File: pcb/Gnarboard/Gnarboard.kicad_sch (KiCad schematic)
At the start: 2 parts, among them U2 MCP3208

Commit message: a bit more progress on the design. kicad pretty decent these days.
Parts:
- added C1: 100nF, Capacitor_THT:C_Disc_D4.7mm_W2.5mm_P5.00mm, symbol Device:C_Small
- added C2: 100uF, Capacitor_THT:CP_Radial_D8.0mm_P5.00mm, symbol Device:C_Polarized_Small
- added D1: 30V, Diode_THT:D_DO-35_SOD27_P10.16mm_Horizontal, symbol Diode:ZPDxx
- added U3: ~, gnarboard:DF1768, symbol gnarboard:DFR0571
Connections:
- net +3.3V: now also C1.1, C2.1, U3.1 (VOUT1+), U3.2 (VOUT+2)
- net GNDA: now also U3.4 (GND4)
- net GNDD: now also C1.2, C2.2, U3.3 (GND3)
- net +5V: no longer names the net of U1.19 (5V0)
- new net +24V: D1.1 (K), U3.7 (VIN+2), U3.8 (VIN+1)
- new net GNDPWR: D1.2 (A), U3.5 (GND2), U3.6 (GND1)

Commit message: added pololu regulator. loving kicad.
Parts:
- added U4: D24V5F3, gnarboard:D24V5FX, symbol gnarboard:DF24V5Fx
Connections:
- net +24V: now also U4.2 (VIN), U4.3 (GND)
- net +3.3V: now also U4.4 (VOUT)
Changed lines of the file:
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@@
   (junction (at 115.57 48.26) (diameter 0) (color 0 0 0 0)
   )
+  (junction (at 33.02 45.72) (diameter 0) (color 0 0 0 0)
+  )
   (junction (at 76.2 48.26) (diameter 0) (color 0 0 0 0)
   )
@@
   (junction (at 76.2 53.34) (diameter 0) (color 0 0 0 0)
   )
+  (junction (at 97.79 48.26) (diameter 0) (color 0 0 0 0)
+  )
   (junction (at 39.37 45.72) (diameter 0) (color 0 0 0 0)
   )
   (junction (at 185.42 48.26) (diameter 0) (color 0 0 0 0)
   )
+  (junction (at 27.94 77.47) (diameter 0) (color 0 0 0 0)
+  )
   (wire (pts (xy 33.02 45.72) (xy 33.02 46.99))
     (stroke (width 0) (type default))
@@
     (stroke (width 0) (type default))
   )
+  (wire (pts (xy 45.72 77.47) (xy 27.94 77.47))
+    (stroke (width 0) (type default))
+  )
   (wire (pts (xy 43.18 55.88) (xy 39.37 55.88))
     (stroke (width 0) (type default))
@@
     (stroke (width 0) (type default))
   )
-  (wire (pts (xy 87.63 48.26) (xy 115.57 48.26))
+  (wire (pts (xy 97.79 48.26) (xy 115.57 48.26))
+    (stroke (width 0) (type default))
+  )
+  (wire (pts (xy 27.94 45.72) (xy 33.02 45.72))
+    (stroke (width 0) (type default))
+  )
+  (wire (pts (xy 87.63 48.26) (xy 97.79 48.26))
     (stroke (width 0) (type default))
   )
@@
     (stroke (width 0) (type default))
   )
+  (wire (pts (xy 66.04 77.47) (xy 97.79 77.47))
+    (stroke (width 0) (type default))
+  )
   (wire (pts (xy 33.02 55.88) (xy 33.02 54.61))
     (stroke (width 0) (type default))
@@
     (stroke (width 0) (type default))
   )
+  (wire (pts (xy 27.94 87.63) (xy 27.94 77.47))
+    (stroke (width 0) (type default))
+  )
   (wire (pts (xy 172.72 80.01) (xy 175.26 80.01))
     (stroke (width 0) (type default))
@@
     (stroke (width 0) (type default))
   )
+  (wire (pts (xy 55.88 87.63) (xy 27.94 87.63))
+    (stroke (width 0) (type default))
+  )
   (wire (pts (xy 76.2 48.26) (xy 87.63 48.26))
     (stroke (width 0) (type default))
@@
   )
   (wire (pts (xy 68.58 45.72) (xy 71.12 45.72))
+    (stroke (width 0) (type default))
+  )
+  (wire (pts (xy 97.79 77.47) (xy 97.79 48.26))
+    (stroke (width 0) (type default))
+  )
+  (wire (pts (xy 27.94 77.47) (xy 27.94 45.72))
     (stroke (width 0) (type default))
   )
@@
         )
       )
+    )
+  )
+  (symbol (lib_id "gnarboard:DF24V5Fx") (at 55.88 78.74 0) (unit 1)
+    (in_bom yes) (on_board yes) (dnp no) (fields_autoplaced)
+    (property "Reference" "U4" (at 55.88 71.12 0)
+      (effects (font (size 1.27 1.27)))
+    )
+    (property "Value" "D24V5F3" (at 55.88 74.93 0)
+      (effects (font (size 1.27 1.27)))
+    )
+    (property "Footprint" "gnarboard:D24V5FX" (at 55.88 74.93 0)
+      (effects (font (size 1.27 1.27)) hide)
+    )
+    (property "Datasheet" "" (at 55.88 74.93 0)
+      (effects (font (size 1.27 1.27)) hide)
+    )
+    (pin "1")
+    (pin "2")
+    (pin "3")
+    (pin "4")
+    (instances
+      (project "Gnarboard"
+        (path "/c83c6236-96e9-46ad-9d7a-9e2efa4a7966"
+          (reference "U4") (unit 1)
+        )
+      )

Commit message: much progresso en schematico
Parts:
- added C3: 1nF, Capacitor_SMD:C_0805_2012Metric_Pad1.18x1.45mm_HandSolder, symbol Device:C_Small
- added C4: 4.7nF, Capacitor_SMD:C_0805_2012Metric_Pad1.18x1.45mm_HandSolder, symbol Device:C_Small
- added C5: 100nF, Capacitor_SMD:C_0805_2012Metric_Pad1.18x1.45mm_HandSolder, symbol Device:C_Small
- added D2: LED, LED_SMD:LED_0805_2012Metric_Pad1.15x1.40mm_HandSolder, symbol Device:LED
- added F1: 25A, gnarboard:ATC Bypass Fuse, symbol gnarboard:ATC Fuse Bypass
- added J1, J2, J3, J4: Screw_Terminal_01x08, Connector_Phoenix_GMSTB:PhoenixContact_GMSTBVA_2,5_8-G_1x08_P7.50mm_Vertical, symbol Connector:Screw_Terminal_01x08
- added Q1: IRF4905, Package_TO_SOT_SMD:TO-263-2, symbol Transistor_FET:IRF4905
- added Q2: MMBT5551L, Package_TO_SOT_SMD:SOT-23, symbol Transistor_BJT:MMBT5551L
- added R1, R4: 10k, Resistor_SMD:R_0805_2012Metric_Pad1.20x1.40mm_HandSolder, symbol Device:R_Small_US
- added R2: 1k, Resistor_SMD:R_0805_2012Metric_Pad1.20x1.40mm_HandSolder, symbol Device:R_Small_US
- added R3: 100k, Resistor_SMD:R_0805_2012Metric_Pad1.20x1.40mm_HandSolder, symbol Device:R_Small_US
- added U5: ACS725xLCTR-20AU, Package_SO:SOIC-8_3.9x4.9mm_P1.27mm, symbol Sensor_Current:ACS725xLCTR-20AU
- C1: footprint Capacitor_THT:C_Disc_D4.7mm_W2.5mm_P5.00mm -> Capacitor_SMD:C_0805_2012Metric_Pad1.18x1.45mm_HandSolder
- U2: footprint Package_DIP:DIP-16_W7.62mm -> Package_SO:SOIC-16_3.9x9.9mm_P1.27mm
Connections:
- net +24V: now also F1.2, J3.1 (Pin_1), J3.2 (Pin_2), J3.3 (Pin_3), J3.4 (Pin_4), J3.5 (Pin_5), J3.6 (Pin_6), J3.7 (Pin_7), J3.8 (Pin_8), R4.2
- net +3.3V: now also C5.1, U5.8 (VCC)
- net GNDA: now also C3.2, C4.2, C5.2, U5.5 (GND)
- net GNDD: now also D2.1 (K), Q2.2 (E)
- net GNDPWR: now also J4.1 (Pin_1), J4.2 (Pin_2), J4.3 (Pin_3), J4.4 (Pin_4), J4.5 (Pin_5), J4.6 (Pin_6), J4.7 (Pin_7), J4.8 (Pin_8), U5.3 (IP-), U5.4 (IP-)
- net ADC0: now reaches U2.1 (CH0)
- net ADC0: now also C4.1, U5.7 (VIOUT)
- net ADC1: now reaches U2.2 (CH1)
- net ADC2: now reaches U2.3 (CH2)
- net ADC3: now reaches U2.4 (CH3)
- net ADC4: now reaches U2.5 (CH4)
- net ADC5: now reaches U2.6 (CH5)
- net ADC6: now reaches U2.7 (CH6)
- net ADC7: now reaches U2.8 (CH7)
- net PWM3: now reaches U1.10 (GPIO26)
- net PWM4: now reaches U1.11 (GPIO27)
- net PWM5: now reaches U1.12 (GPIO14)
- net PWM6: now reaches U1.13 (GPIO12)
- net PWM7: now reaches U1.15 (GPIO13)
- net PWM0: now reaches U1.7 (GPIO32)
- net PWM0: now also R1.1, R2.2
- net PWM1: now reaches U1.8 (GPIO33)
- net PWM2: now reaches U1.9 (GPIO25)
- new net: Q2.1 (B), R1.2
- new net: Q2.3 (C), R3.1
- new net: F1.1, Q1.3 (S)
- new net: C3.1, U5.6 (FILTER)
- new net: D2.2 (A), R2.1
- new net: Q1.1 (G), R3.2, R4.1
- new net CH0+: F1.3, J1.1 (Pin_1), Q1.2 (D)
- new net CH0-: J1.2 (Pin_2), U5.1 (IP+), U5.2 (IP+)
- new net CH1+: J1.3 (Pin_3)
- new net CH1-: J1.4 (Pin_4)
- new net CH2+: J1.5 (Pin_5)
- new net CH2-: J1.6 (Pin_6)
- new net CH3+: J1.7 (Pin_7)
- new net CH3-: J1.8 (Pin_8)
- new net CH4+: J2.1 (Pin_1)
- new net CH4-: J2.2 (Pin_2)
- new net CH5+: J2.3 (Pin_3)
- new net CH5-: J2.4 (Pin_4)
- new net CH6+: J2.5 (Pin_5)
- new net CH6-: J2.6 (Pin_6)
- new net CH7+: J2.7 (Pin_7)
- new net CH7-: J2.8 (Pin_8)
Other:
- note added: "Current Sensing"
- note added: "MOSFET"

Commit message: wow, kicad hierarchical sheets... epic.
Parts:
- removed C3: 1nF, Capacitor_SMD:C_0805_2012Metric_Pad1.18x1.45mm_HandSolder, symbol Device:C_Small
- removed C4: 4.7nF, Capacitor_SMD:C_0805_2012Metric_Pad1.18x1.45mm_HandSolder, symbol Device:C_Small
- removed C5: 100nF, Capacitor_SMD:C_0805_2012Metric_Pad1.18x1.45mm_HandSolder, symbol Device:C_Small
- removed D2: LED, LED_SMD:LED_0805_2012Metric_Pad1.15x1.40mm_HandSolder, symbol Device:LED
- removed F1: 25A, gnarboard:ATC Bypass Fuse, symbol gnarboard:ATC Fuse Bypass
- removed Q1: IRF4905, Package_TO_SOT_SMD:TO-263-2, symbol Transistor_FET:IRF4905
- removed Q2: MMBT5551L, Package_TO_SOT_SMD:SOT-23, symbol Transistor_BJT:MMBT5551L
- removed R1, R4: 10k, Resistor_SMD:R_0805_2012Metric_Pad1.20x1.40mm_HandSolder, symbol Device:R_Small_US
- removed R2: 1k, Resistor_SMD:R_0805_2012Metric_Pad1.20x1.40mm_HandSolder, symbol Device:R_Small_US
- removed R3: 100k, Resistor_SMD:R_0805_2012Metric_Pad1.20x1.40mm_HandSolder, symbol Device:R_Small_US
- removed U5: ACS725xLCTR-20AU, Package_SO:SOIC-8_3.9x4.9mm_P1.27mm, symbol Sensor_Current:ACS725xLCTR-20AU
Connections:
- net ADC0 renamed CHANNEL 0/ADC
- net ADC1 renamed CHANNEL 1/ADC
- net ADC2 renamed CHANNEL 2/ADC
- net ADC3 renamed CHANNEL 3/ADC
- net ADC4 renamed CHANNEL 4/ADC
- net ADC5 renamed CHANNEL 5/ADC
- net ADC6 renamed CHANNEL 6/ADC
- net ADC7 renamed CHANNEL 7/ADC
- net CH0+ renamed CHANNEL 0/LOAD-
- net CH0- renamed CHANNEL 0/LOAD+
- net CH1+ renamed CHANNEL 1/LOAD-
- net CH1- renamed CHANNEL 1/LOAD+
- net CH2+ renamed CHANNEL 2/LOAD-
- net CH2- renamed CHANNEL 2/LOAD+
- net CH3+ renamed CHANNEL 3/LOAD-
- net CH3- renamed CHANNEL 3/LOAD+
- net CH4+ renamed CHANNEL 4/LOAD-
- net CH4- renamed CHANNEL 4/LOAD+
- net CH5+ renamed CHANNEL 5/LOAD-
- net CH5- renamed CHANNEL 5/LOAD+
- net CH6+ renamed CHANNEL 6/LOAD-
- net CH6- renamed CHANNEL 6/LOAD+
- net CH7+ renamed CHANNEL 7/LOAD-
- net CH7- renamed CHANNEL 7/LOAD+
- net PWM0 renamed CHANNEL 0/PWM
- net PWM1 renamed CHANNEL 1/PWM
- net PWM2 renamed CHANNEL 2/PWM
- net PWM3 renamed CHANNEL 3/PWM
- net PWM4 renamed CHANNEL 4/PWM
- net PWM5 renamed CHANNEL 5/PWM
- net PWM6 renamed CHANNEL 6/PWM
- net PWM7 renamed CHANNEL 7/PWM
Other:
- added sheet CHANNEL 0 (mosfet.kicad_sch)
- added sheet CHANNEL 1 (mosfet.kicad_sch)
- added sheet CHANNEL 2 (mosfet.kicad_sch)
- added sheet CHANNEL 3 (mosfet.kicad_sch)
- added sheet CHANNEL 4 (mosfet.kicad_sch)
- added sheet CHANNEL 5 (mosfet.kicad_sch)
- added sheet CHANNEL 6 (mosfet.kicad_sch)
- added sheet CHANNEL 7 (mosfet.kicad_sch)
- note removed: "Current Sensing"
- note removed: "MOSFET"
- moved on the sheet: C1, C2, D1, J1, J2, J3, J4, U1, U2, U3, U4

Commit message: big kicad progress.
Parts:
- removed C2: 100uF, Capacitor_THT:CP_Radial_D8.0mm_P5.00mm, symbol Device:C_Polarized_Small
- removed J3, J4: Screw_Terminal_01x08, Connector_Phoenix_GMSTB:PhoenixContact_GMSTBVA_2,5_8-G_1x08_P7.50mm_Vertical, symbol Connector:Screw_Terminal_01x08
- added J3, J4: Screw_Terminal_01x12, gnarboard:BSS 2301, symbol Connector:Screw_Terminal_01x12
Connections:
- net +24V: now also J3.1 (Pin_1), J3.10 (Pin_10), J3.11 (Pin_11), J3.12 (Pin_12), J3.2 (Pin_2), J3.3 (Pin_3), J3.4 (Pin_4), J3.5 (Pin_5), J3.6 (Pin_6), J3.7 (Pin_7), J3.8 (Pin_8), J3.9 (Pin_9)
- net GNDPWR: now also J4.1 (Pin_1), J4.10 (Pin_10), J4.11 (Pin_11), J4.12 (Pin_12), J4.2 (Pin_2), J4.3 (Pin_3), J4.4 (Pin_4), J4.5 (Pin_5), J4.6 (Pin_6), J4.7 (Pin_7), J4.8 (Pin_8), J4.9 (Pin_9)
- net CHANNEL 0/ADC renamed ADC0
- net CHANNEL 0/LOAD+ renamed CH-0
- net CHANNEL 0/LOAD- renamed CH+0
- net CHANNEL 0/PWM renamed PWM0
- net CHANNEL 1/ADC renamed ADC1
- net CHANNEL 1/LOAD+ renamed CH-1
- net CHANNEL 1/LOAD- renamed CH+1
- net CHANNEL 1/PWM renamed PWM1
- net CHANNEL 2/ADC renamed ADC2
- net CHANNEL 2/LOAD+ renamed CH-2
- net CHANNEL 2/LOAD- renamed CH+2
- net CHANNEL 2/PWM renamed PWM2
- net CHANNEL 3/ADC renamed ADC3
- net CHANNEL 3/LOAD+ renamed CH-3
- net CHANNEL 3/LOAD- renamed CH+3
- net CHANNEL 3/PWM renamed PWM3
- net CHANNEL 4/ADC renamed ADC4
- net CHANNEL 4/LOAD+ renamed CH-4
- net CHANNEL 4/LOAD- renamed CH+4
- net CHANNEL 4/PWM renamed PWM4
- net CHANNEL 5/ADC renamed ADC5
- net CHANNEL 5/LOAD+ renamed CH-5
- net CHANNEL 5/LOAD- renamed CH+5
- net CHANNEL 5/PWM renamed PWM5
- net CHANNEL 6/ADC renamed ADC6
- net CHANNEL 6/LOAD+ renamed CH-6
- net CHANNEL 6/LOAD- renamed CH+6
- net CHANNEL 6/PWM renamed PWM6
- net CHANNEL 7/ADC renamed ADC7
- net CHANNEL 7/LOAD+ renamed CH-7
- net CHANNEL 7/LOAD- renamed CH+7
- net CHANNEL 7/PWM renamed PWM7
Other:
- moved on the sheet: J1, J2

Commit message: board mostly laid out.
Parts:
- added JP1, JP2: SolderJumper_2_Bridged, Jumper:SolderJumper-2_P1.3mm_Bridged_RoundedPad1.0x1.5mm, symbol Jumper:SolderJumper_2_Bridged
- D1: footprint Diode_THT:D_DO-35_SOD27_P10.16mm_Horizontal -> Diode_SMD:D_SOD-123
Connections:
- net +24V: no longer U4.3 (GND)
- net GNDA: now also JP1.2 (B); no longer U3.4 (GND4)
- net GNDD: now also D1.2 (A), U3.4 (GND4), U3.5 (GND2), U3.6 (GND1), U4.3 (GND), JP1.1 (A), JP2.2 (B)
- net GNDPWR: now also JP2.1 (A); no longer D1.2 (A), U3.5 (GND2), U3.6 (GND1)

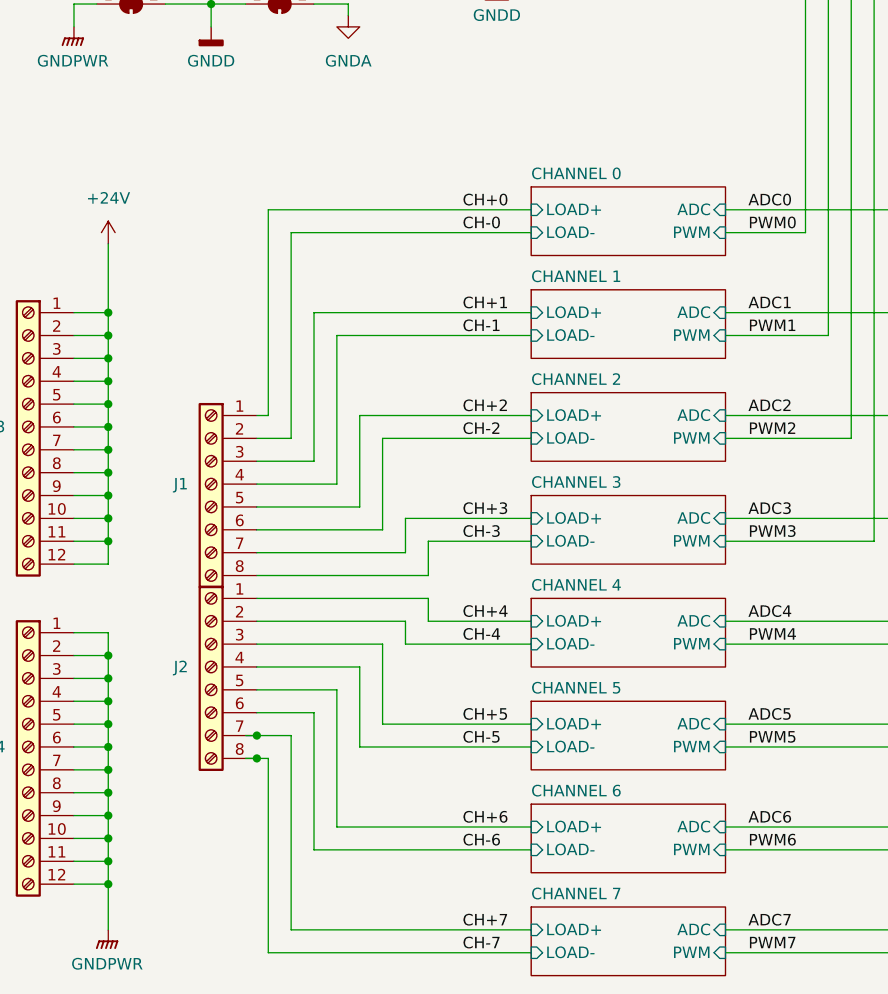
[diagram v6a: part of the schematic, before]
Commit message: board close to being ready for a prototype
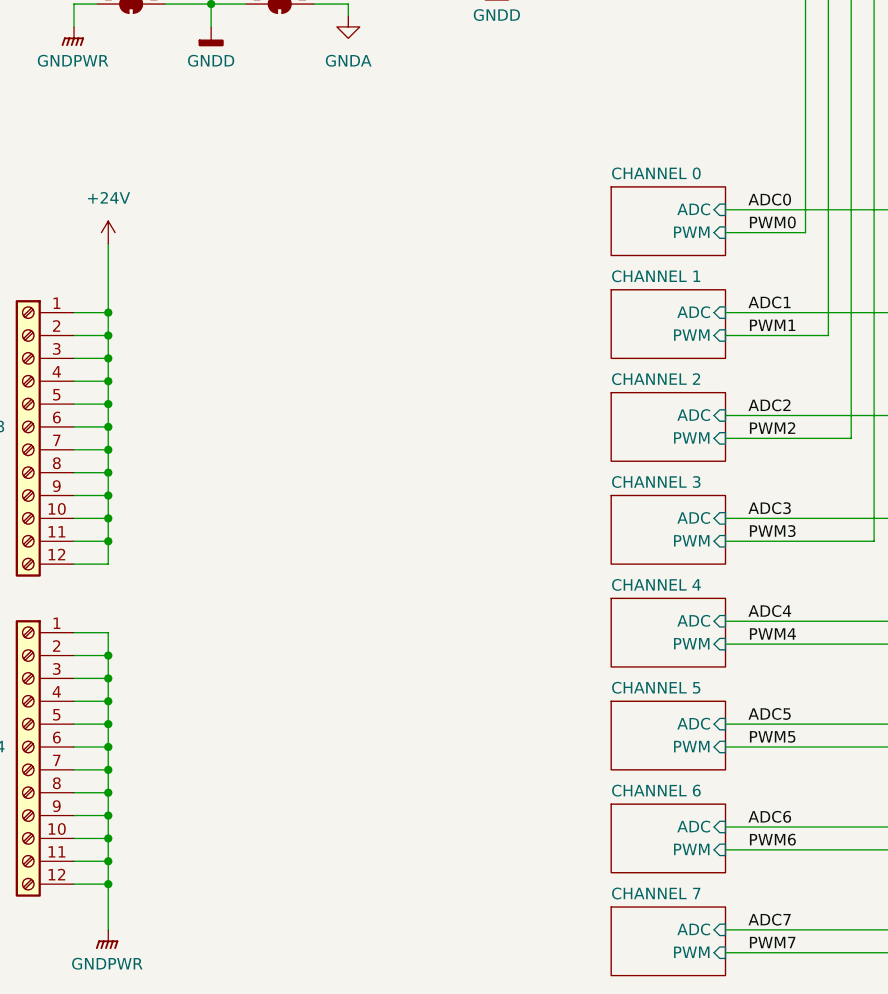
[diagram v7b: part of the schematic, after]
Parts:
- removed J1, J2: Screw_Terminal_01x08, Connector_Phoenix_GMSTB:PhoenixContact_GMSTBVA_2,5_8-G_1x08_P7.50mm_Vertical, symbol Connector:Screw_Terminal_01x08
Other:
- sheet CHANNEL 0 ports: added none; removed LOAD+, LOAD-
- sheet CHANNEL 1 ports: added none; removed LOAD+, LOAD-
- sheet CHANNEL 2 ports: added none; removed LOAD+, LOAD-
- sheet CHANNEL 3 ports: added none; removed LOAD+, LOAD-
- sheet CHANNEL 4 ports: added none; removed LOAD+, LOAD-
- sheet CHANNEL 5 ports: added none; removed LOAD+, LOAD-
- sheet CHANNEL 6 ports: added none; removed LOAD+, LOAD-
- sheet CHANNEL 7 ports: added none; removed LOAD+, LOAD-

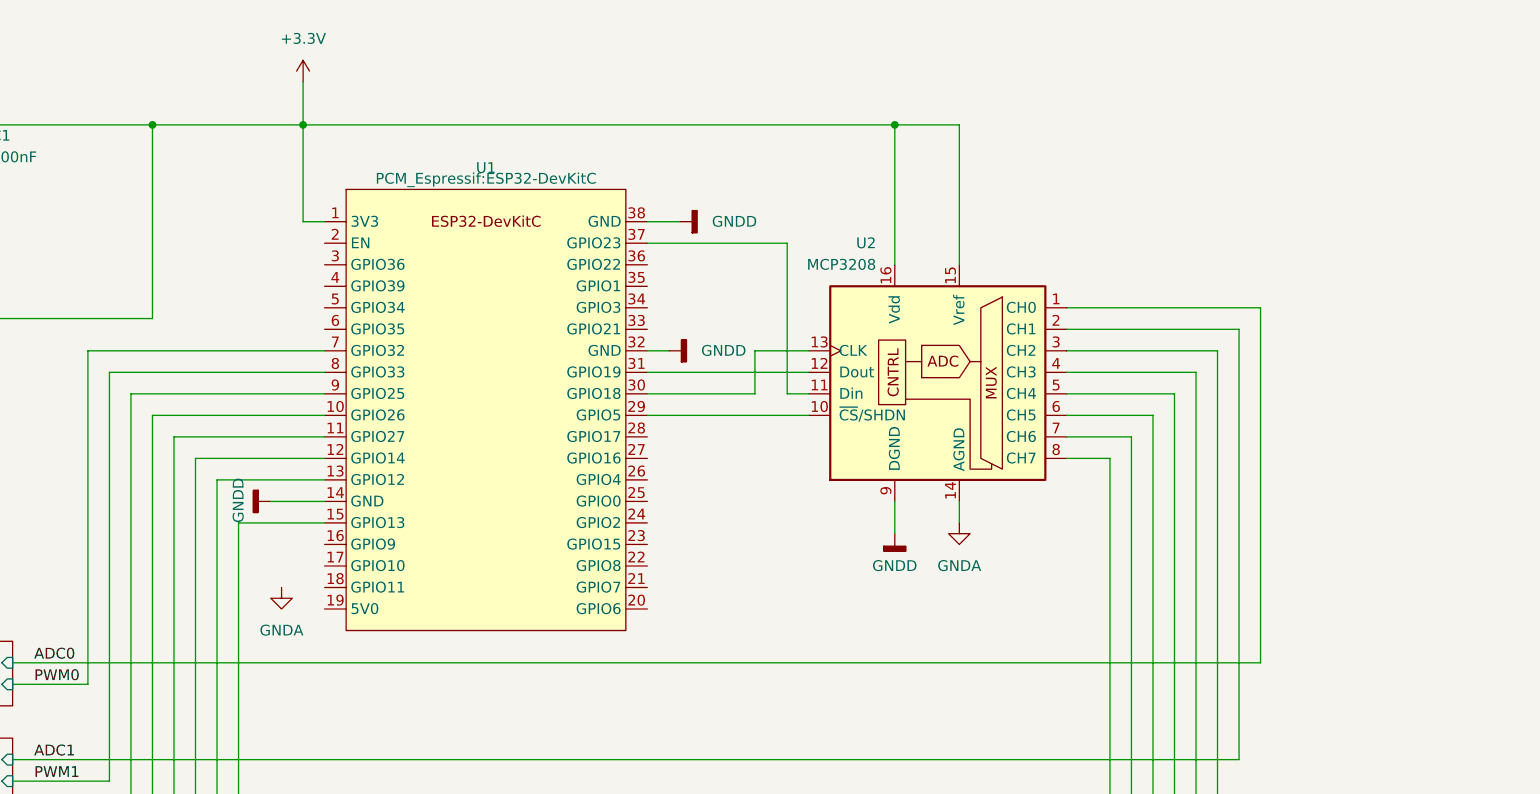
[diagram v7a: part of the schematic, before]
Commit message: added a qwiic connector
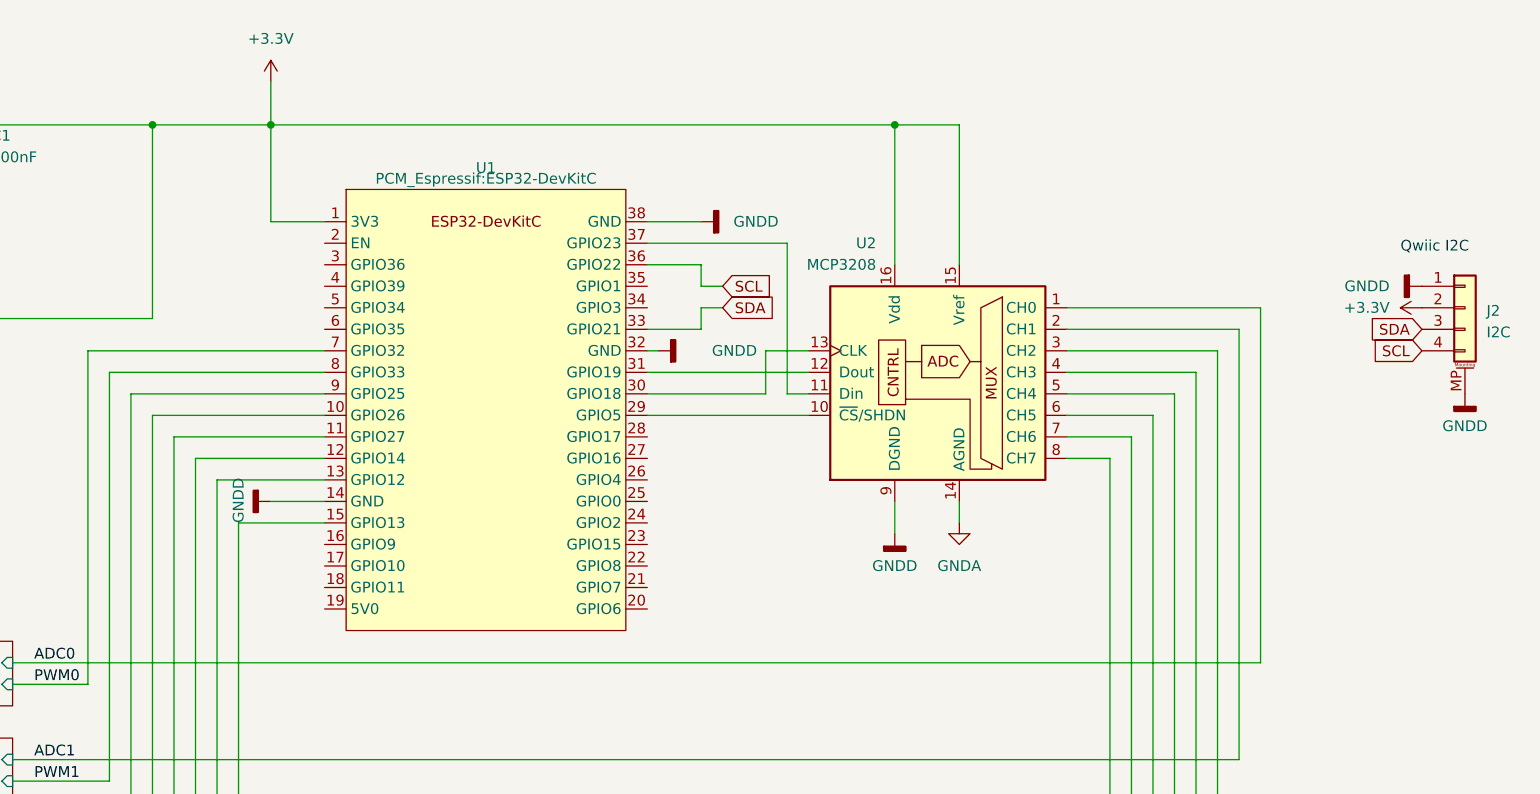
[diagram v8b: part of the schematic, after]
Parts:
- added J2: I2C, Connector_JST:JST_SH_SM04B-SRSS-TB_1x04-1MP_P1.00mm_Horizontal, symbol Connector_Generic_MountingPin:Conn_01x04_MountingPin
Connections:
- net +3.3V: now also J2.2 (Pin_2)
- net GNDD: now also J2.1 (Pin_1), J2.MP (MountPin)
- net SDA: now reaches U1.33 (GPIO21)
- net SDA: now also J2.3 (Pin_3)
- net SCL: now reaches U1.36 (GPIO22)
- net SCL: now also J2.4 (Pin_4)
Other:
- note added: "Qwiic I2C"
